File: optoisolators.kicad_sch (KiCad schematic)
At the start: 17 parts, among them J8 Conn_01x06_Female, J9 Conn_01x06_Female, U12 VO615A, U13 VO615A, U14 VO615A, U15 VO615A, U16 VO615A, U17 VO615A

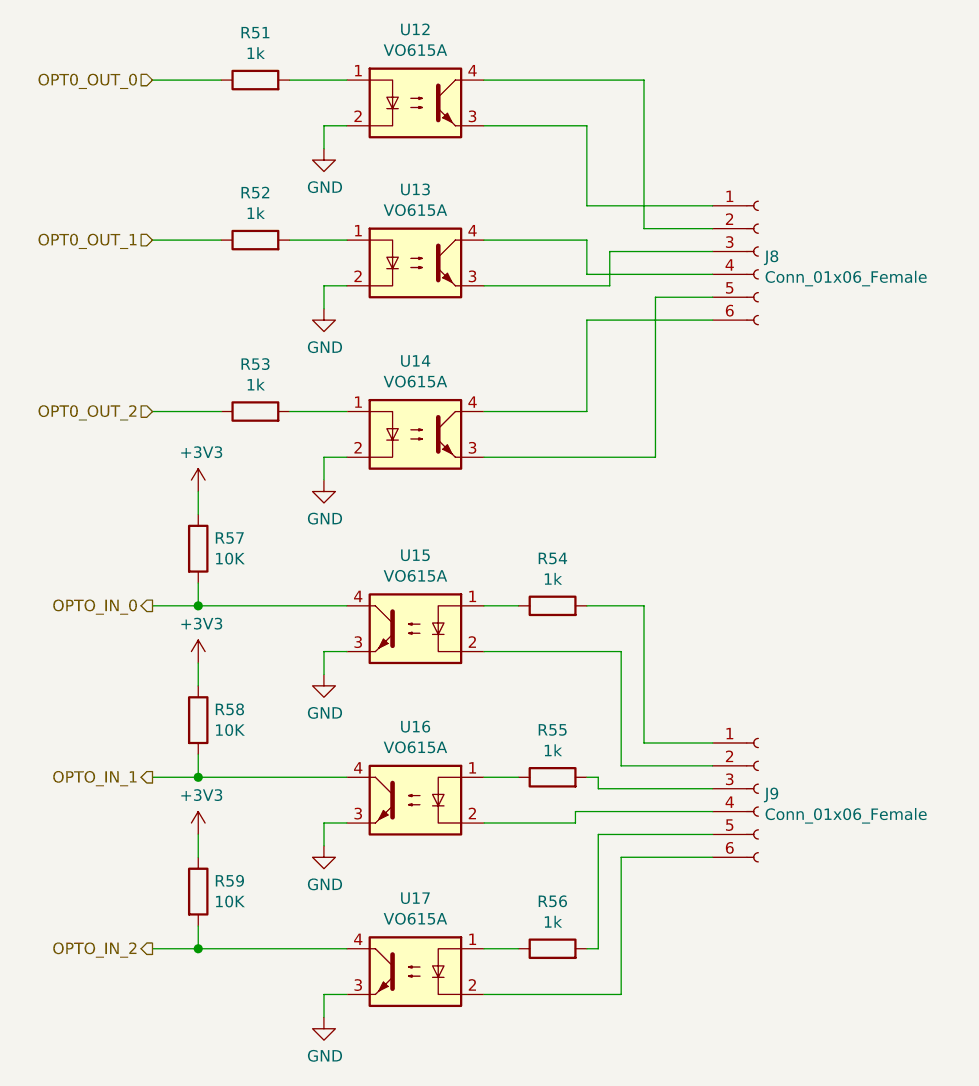
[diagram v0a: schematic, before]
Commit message: Finished tidying up silkscreen
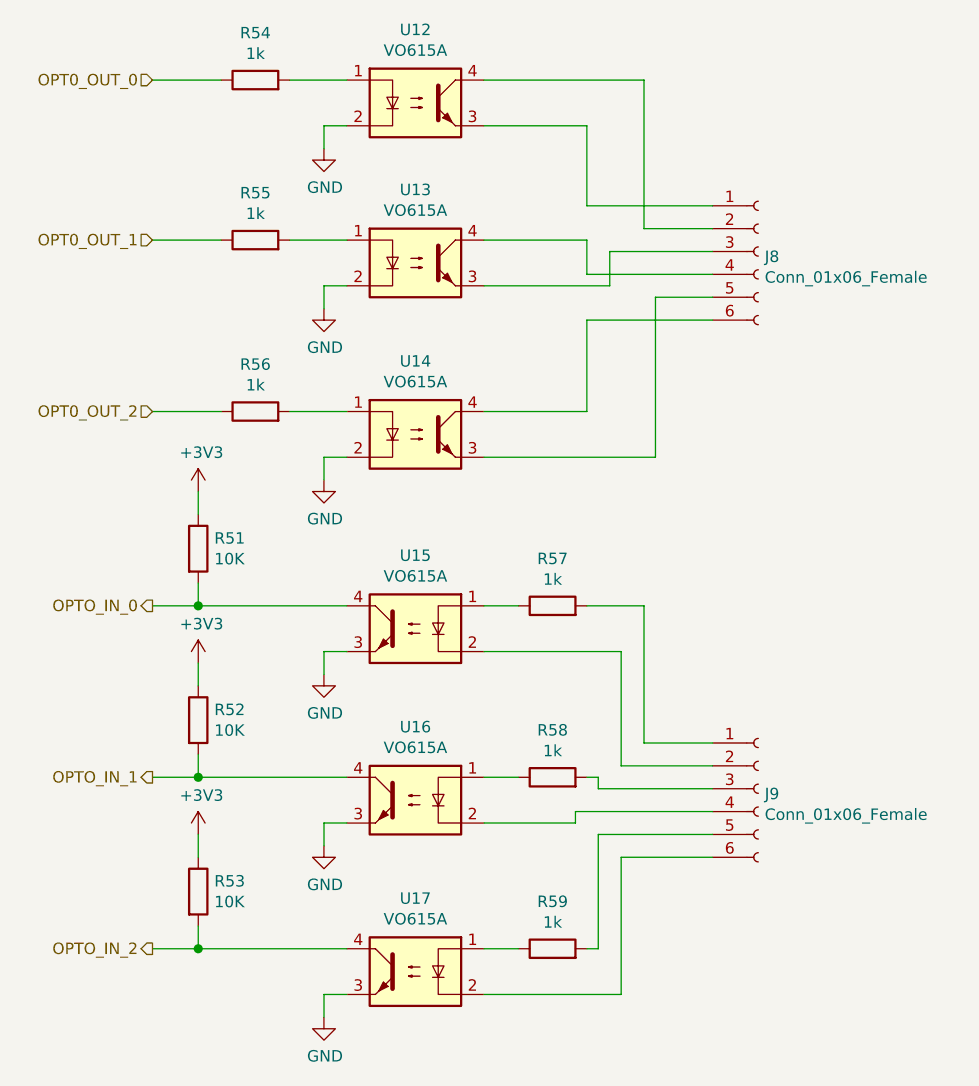
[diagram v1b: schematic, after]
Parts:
- renumbered R57 to R51, R58 to R52, R59 to R53, R51 to R54, R52 to R55, R53 to R56, R54 to R57, R55 to R58, R56 to R59
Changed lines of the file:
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@@
   (symbol (lib_id "power:+3V3") (at 123.19 93.98 0) (unit 1)
     (in_bom yes) (on_board yes)
-    (property "Reference" "#PWR0104" (id 0) (at 123.19 97.79 0)
+    (property "Reference" "#PWR098" (id 0) (at 123.19 97.79 0)
       (effects (font (size 1.27 1.27)) hide)
     )
@@
   (symbol (lib_id "power:+3V3") (at 123.19 113.03 0) (unit 1)
     (in_bom yes) (on_board yes)
-    (property "Reference" "#PWR0106" (id 0) (at 123.19 116.84 0)
+    (property "Reference" "#PWR099" (id 0) (at 123.19 116.84 0)
       (effects (font (size 1.27 1.27)) hide)
     )
@@
   (symbol (lib_id "power:+3V3") (at 123.19 132.08 0) (unit 1)
     (in_bom yes) (on_board yes)
-    (property "Reference" "#PWR0105" (id 0) (at 123.19 135.89 0)
+    (property "Reference" "#PWR0100" (id 0) (at 123.19 135.89 0)
       (effects (font (size 1.27 1.27)) hide)
     )
@@
   (symbol (lib_id "power:GND") (at 137.16 55.88 0) (unit 1)
     (in_bom yes) (on_board yes)
-    (property "Reference" "#PWR098" (id 0) (at 137.16 62.23 0)
+    (property "Reference" "#PWR0101" (id 0) (at 137.16 62.23 0)
       (effects (font (size 1.27 1.27)) hide)
     )
@@
   (symbol (lib_id "power:GND") (at 137.16 73.66 0) (unit 1)
     (in_bom yes) (on_board yes)
-    (property "Reference" "#PWR099" (id 0) (at 137.16 80.01 0)
+    (property "Reference" "#PWR0102" (id 0) (at 137.16 80.01 0)
       (effects (font (size 1.27 1.27)) hide)
     )
@@
   (symbol (lib_id "power:GND") (at 137.16 92.71 0) (unit 1)
     (in_bom yes) (on_board yes)
-    (property "Reference" "#PWR0100" (id 0) (at 137.16 99.06 0)
+    (property "Reference" "#PWR0103" (id 0) (at 137.16 99.06 0)
       (effects (font (size 1.27 1.27)) hide)
     )
@@
   (symbol (lib_id "power:GND") (at 137.16 114.3 0) (unit 1)
     (in_bom yes) (on_board yes)
-    (property "Reference" "#PWR0101" (id 0) (at 137.16 120.65 0)
+    (property "Reference" "#PWR0104" (id 0) (at 137.16 120.65 0)
       (effects (font (size 1.27 1.27)) hide)
     )
@@
   (symbol (lib_id "power:GND") (at 137.16 133.35 0) (unit 1)
     (in_bom yes) (on_board yes)
-    (property "Reference" "#PWR0102" (id 0) (at 137.16 139.7 0)
+    (property "Reference" "#PWR0105" (id 0) (at 137.16 139.7 0)
       (effects (font (size 1.27 1.27)) hide)
     )
@@
   (symbol (lib_id "power:GND") (at 137.16 152.4 0) (unit 1)
     (in_bom yes) (on_board yes)
-    (property "Reference" "#PWR0103" (id 0) (at 137.16 158.75 0)
+    (property "Reference" "#PWR0106" (id 0) (at 137.16 158.75 0)
       (effects (font (size 1.27 1.27)) hide)
     )
@@
   (symbol (lib_id "Device:R") (at 123.19 100.33 0) (unit 1)
     (in_bom yes) (on_board yes)
-    (property "Reference" "R57" (id 0) (at 124.9681 99.1806 0)
+    (property "Reference" "R51" (id 0) (at 124.9681 99.1806 0)
       (effects (font (size 1.27 1.27)) (justify left))
     )
@@
   (symbol (lib_id "Device:R") (at 123.19 119.38 0) (unit 1)
     (in_bom yes) (on_board yes)
-    (property "Reference" "R58" (id 0) (at 124.9681 118.2306 0)
+    (property "Reference" "R52" (id 0) (at 124.9681 118.2306 0)
       (effects (font (size 1.27 1.27)) (justify left))
     )
@@
   (symbol (lib_id "Device:R") (at 123.19 138.43 0) (unit 1)
     (in_bom yes) (on_board yes)
-    (property "Reference" "R59" (id 0) (at 124.9681 137.2806 0)
+    (property "Reference" "R53" (id 0) (at 124.9681 137.2806 0)
       (effects (font (size 1.27 1.27)) (justify left))
     )
@@
   (symbol (lib_id "Device:R") (at 129.54 48.26 90) (unit 1)
     (in_bom yes) (on_board yes)
-    (property "Reference" "R51" (id 0) (at 129.54 43.0338 90))
+    (property "Reference" "R54" (id 0) (at 129.54 43.0338 90))
     (property "Value" "1k" (id 1) (at 129.54 45.332 90))
     (property "Footprint" "Resistor_SMD:R_0603_1608Metric" (id 2) (at 129.54 50.038 90)
@@
   (symbol (lib_id "Device:R") (at 129.54 66.04 90) (unit 1)
     (in_bom yes) (on_board yes)
-    (property "Reference" "R52" (id 0) (at 129.54 60.8138 90))
+    (property "Reference" "R55" (id 0) (at 129.54 60.8138 90))
     (property "Value" "1k" (id 1) (at 129.54 63.112 90))
     (property "Footprint" "Resistor_SMD:R_0603_1608Metric" (id 2) (at 129.54 67.818 90)
@@
   (symbol (lib_id "Device:R") (at 129.54 85.09 90) (unit 1)
     (in_bom yes) (on_board yes)
-    (property "Reference" "R53" (id 0) (at 129.54 79.8638 90))
+    (property "Reference" "R56" (id 0) (at 129.54 79.8638 90))
     (property "Value" "1k" (id 1) (at 129.54 82.162 90))
     (property "Footprint" "Resistor_SMD:R_0603_1608Metric" (id 2) (at 129.54 86.868 90)
@@
   (symbol (lib_id "Device:R") (at 162.56 106.68 90) (unit 1)
     (in_bom yes) (on_board yes)
-    (property "Reference" "R54" (id 0) (at 162.56 101.4538 90))
+    (property "Reference" "R57" (id 0) (at 162.56 101.4538 90))
     (property "Value" "1k" (id 1) (at 162.56 103.752 90))
     (property "Footprint" "Resistor_SMD:R_0603_1608Metric" (id 2) (at 162.56 108.458 90)
@@
   (symbol (lib_id "Device:R") (at 162.56 125.73 90) (unit 1)
     (in_bom yes) (on_board yes)
-    (property "Reference" "R55" (id 0) (at 162.56 120.5038 90))
+    (property "Reference" "R58" (id 0) (at 162.56 120.5038 90))
     (property "Value" "1k" (id 1) (at 162.56 122.802 90))
     (property "Footprint" "Resistor_SMD:R_0603_1608Metric" (id 2) (at 162.56 127.508 90)
@@
   (symbol (lib_id "Device:R") (at 162.56 144.78 90) (unit 1)
     (in_bom yes) (on_board yes)
-    (property "Reference" "R56" (id 0) (at 162.56 139.5538 90))
+    (property "Reference" "R59" (id 0) (at 162.56 139.5538 90))
     (property "Value" "1k" (id 1) (at 162.56 141.852 90))
     (property "Footprint" "Resistor_SMD:R_0603_1608Metric" (id 2) (at 162.56 146.558 90)

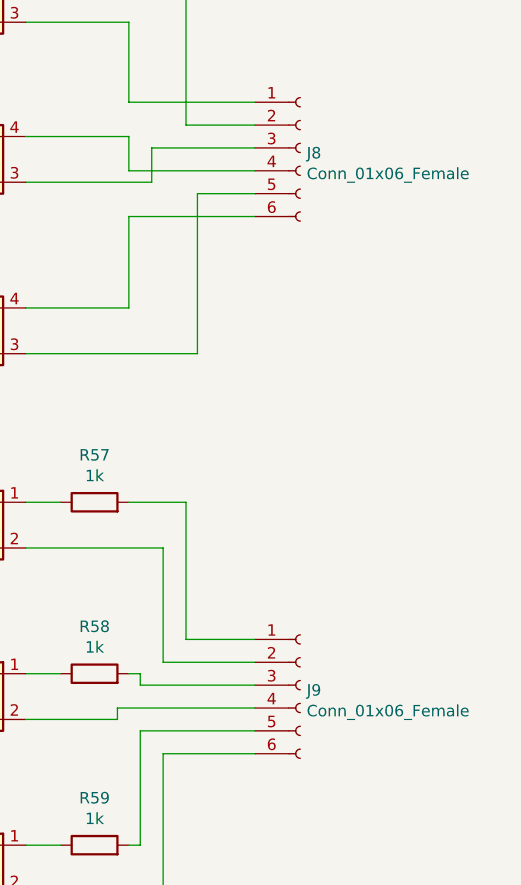
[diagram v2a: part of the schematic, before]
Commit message: Tweaked component values to working. Added rear panel PCB
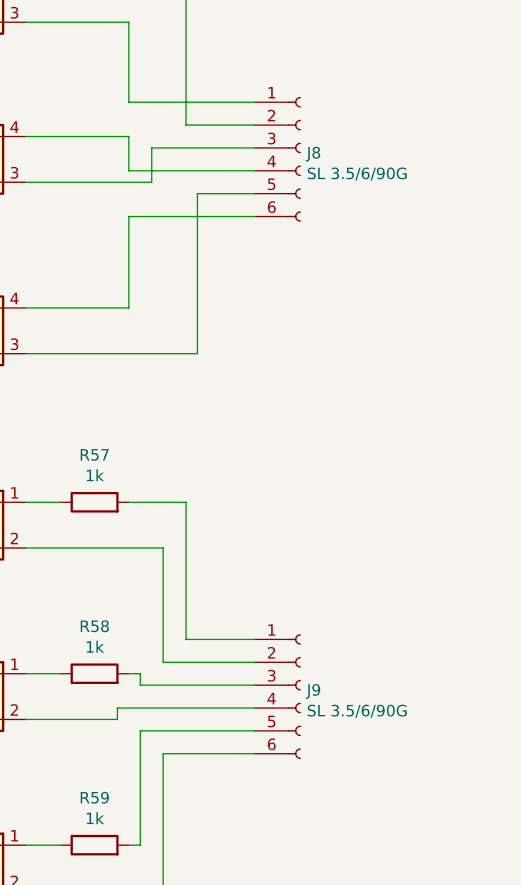
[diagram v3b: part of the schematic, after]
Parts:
- J8, J9: value Conn_01x06_Female -> SL 3.5/6/90G
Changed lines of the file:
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@@
-(kicad_sch (version 20201015) (generator eeschema)
+(kicad_sch (version 20210126) (generator eeschema)
   (paper "A4")
   (junction (at 123.19 106.68) (diameter 1.016) (color 0 0 0 0))
@@
       (effects (font (size 1.27 1.27)) hide)
     )
+    (pin "1")
   )
   (symbol (lib_id "power:+3V3") (at 123.19 113.03 0) (unit 1)
@@
       (effects (font (size 1.27 1.27)) hide)
     )
+    (pin "1")
   )
   (symbol (lib_id "power:+3V3") (at 123.19 132.08 0) (unit 1)
@@
       (effects (font (size 1.27 1.27)) hide)
     )
+    (pin "1")
   )
   (symbol (lib_id "power:GND") (at 137.16 55.88 0) (unit 1)
@@
       (effects (font (size 1.27 1.27)) hide)
     )
+    (pin "1")
   )
   (symbol (lib_id "power:GND") (at 137.16 73.66 0) (unit 1)
@@
       (effects (font (size 1.27 1.27)) hide)
     )
+    (pin "1")
   )
   (symbol (lib_id "power:GND") (at 137.16 92.71 0) (unit 1)
@@
       (effects (font (size 1.27 1.27)) hide)
     )
+    (pin "1")
   )
   (symbol (lib_id "power:GND") (at 137.16 114.3 0) (unit 1)
@@
       (effects (font (size 1.27 1.27)) hide)
     )
+    (pin "1")
   )
   (symbol (lib_id "power:GND") (at 137.16 133.35 0) (unit 1)
@@
       (effects (font (size 1.27 1.27)) hide)
     )
+    (pin "1")
   )
   (symbol (lib_id "power:GND") (at 137.16 152.4 0) (unit 1)
@@
       (effects (font (size 1.27 1.27)) hide)
     )
+    (pin "1")
   )
   (symbol (lib_id "Device:R") (at 123.19 100.33 0) (unit 1)
@@
       (effects (font (size 1.27 1.27)) hide)
     )
+    (pin "1")
+    (pin "2")
   )
   (symbol (lib_id "Device:R") (at 123.19 119.38 0) (unit 1)
@@
       (effects (font (size 1.27 1.27)) hide)
     )
+    (pin "1")
+    (pin "2")
   )
   (symbol (lib_id "Device:R") (at 123.19 138.43 0) (unit 1)
@@
       (effects (font (size 1.27 1.27)) hide)
     )
+    (pin "1")
+    (pin "2")
   )
   (symbol (lib_id "Device:R") (at 129.54 48.26 90) (unit 1)
@@
       (effects (font (size 1.27 1.27)) hide)
     )
+    (pin "1")
+    (pin "2")
   )
   (symbol (lib_id "Device:R") (at 129.54 66.04 90) (unit 1)
@@
       (effects (font (size 1.27 1.27)) hide)
     )
+    (pin "1")
+    (pin "2")
   )
   (symbol (lib_id "Device:R") (at 129.54 85.09 90) (unit 1)
@@
       (effects (font (size 1.27 1.27)) hide)
     )
+    (pin "1")
+    (pin "2")
   )
   (symbol (lib_id "Device:R") (at 162.56 106.68 90) (unit 1)
@@
       (effects (font (size 1.27 1.27)) hide)
     )
+    (pin "1")
+    (pin "2")
   )
   (symbol (lib_id "Device:R") (at 162.56 125.73 90) (unit 1)
@@
       (effects (font (size 1.27 1.27)) hide)
     )
+    (pin "1")
+    (pin "2")
   )
   (symbol (lib_id "Device:R") (at 162.56 144.78 90) (unit 1)
@@
       (effects (font (size 1.27 1.27)) hide)
     )
+    (pin "1")
+    (pin "2")
   )
   (symbol (lib_id "Connector:Conn_01x06_Female") (at 185.42 67.31 0) (unit 1)
@@
       (effects (font (size 1.27 1.27)) (justify left))
     )
-    (property "Value" "Conn_01x06_Female" (id 1) (at 186.1313 70.1865 0)
+    (property "Value" "SL 3.5/6/90G" (id 1) (at 186.131 70.187 0)
       (effects (font (size 1.27 1.27)) (justify left))
     )
@@
       (effects (font (size 1.27 1.27)) hide)
     )
+    (pin "1")
+    (pin "2")
+    (pin "3")
+    (pin "4")
+    (pin "5")
+    (pin "6")
   )
   (symbol (lib_id "Connector:Conn_01x06_Female") (at 185.42 127 0) (unit 1)
@@
       (effects (font (size 1.27 1.27)) (justify left))
     )
-    (property "Value" "Conn_01x06_Female" (id 1) (at 186.1313 129.8765 0)
+    (property "Value" "SL 3.5/6/90G" (id 1) (at 186.131 129.876 0)
       (effects (font (size 1.27 1.27)) (justify left))
     )
@@
       (effects (font (size 1.27 1.27)) hide)
     )
+    (pin "1")
+    (pin "2")
+    (pin "3")
+    (pin "4")
+    (pin "5")
+    (pin "6")
   )
   (symbol (lib_id "Isolator:VO615A") (at 147.32 50.8 0) (unit 1)
@@
       (effects (font (size 1.27 1.27)) hide)
     )
+    (pin "1")
+    (pin "2")
+    (pin "3")
+    (pin "4")
   )
   (symbol (lib_id "Isolator:VO615A") (at 147.32 68.58 0) (unit 1)
@@
       (effects (font (size 1.27 1.27)) hide)
     )
+    (pin "1")
+    (pin "2")
+    (pin "3")
+    (pin "4")
   )
   (symbol (lib_id "Isolator:VO615A") (at 147.32 87.63 0) (unit 1)
@@
       (effects (font (size 1.27 1.27)) hide)
     )
+    (pin "1")
+    (pin "2")
+    (pin "3")
+    (pin "4")
   )
   (symbol (lib_id "Isolator:VO615A") (at 147.32 109.22 0) (mirror y) (unit 1)
@@
       (effects (font (size 1.27 1.27)) hide)
     )
+    (pin "1")
+    (pin "2")
+    (pin "3")
+    (pin "4")
   )
   (symbol (lib_id "Isolator:VO615A") (at 147.32 128.27 0) (mirror y) (unit 1)
@@
       (effects (font (size 1.27 1.27)) hide)
     )
+    (pin "1")
+    (pin "2")
+    (pin "3")
+    (pin "4")
   )
   (symbol (lib_id "Isolator:VO615A") (at 147.32 147.32 0) (mirror y) (unit 1)
@@
       (effects (font (size 1.27 1.27)) hide)
     )
+    (pin "1")
+    (pin "2")
+    (pin "3")
+    (pin "4")
   )
 )
